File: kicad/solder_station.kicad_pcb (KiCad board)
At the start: 2 copper layers, 63.8 x 64 mm, 43 parts, among them IC1 ATMEGA328-P, P1 CONN_01X05, P2 CONN_01X02, P3 Standby, P4 UART, Q1 2N7000, Q2 IRF4905, U1 LM2596_module, U2 AD8551, U3 EC11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

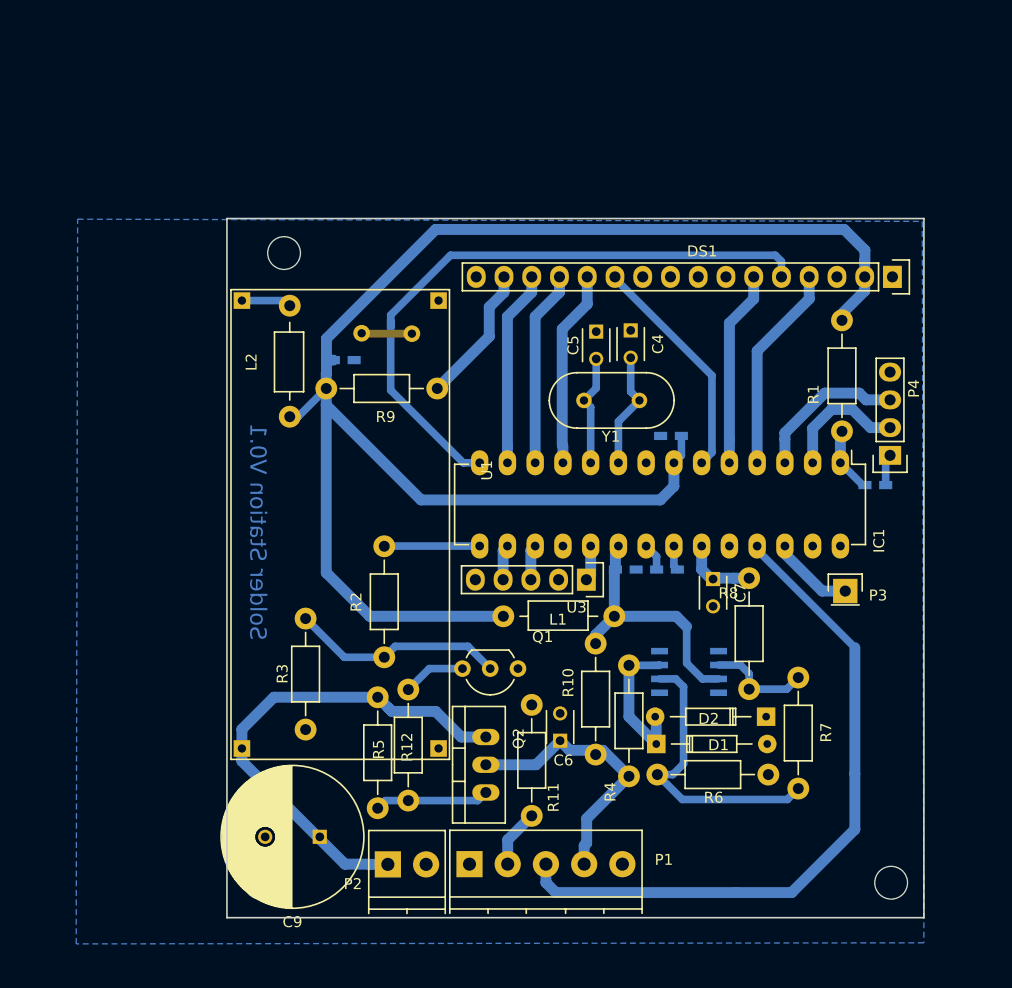
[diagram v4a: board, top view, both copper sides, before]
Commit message: [Kicad] Use more capacitors and smd parts
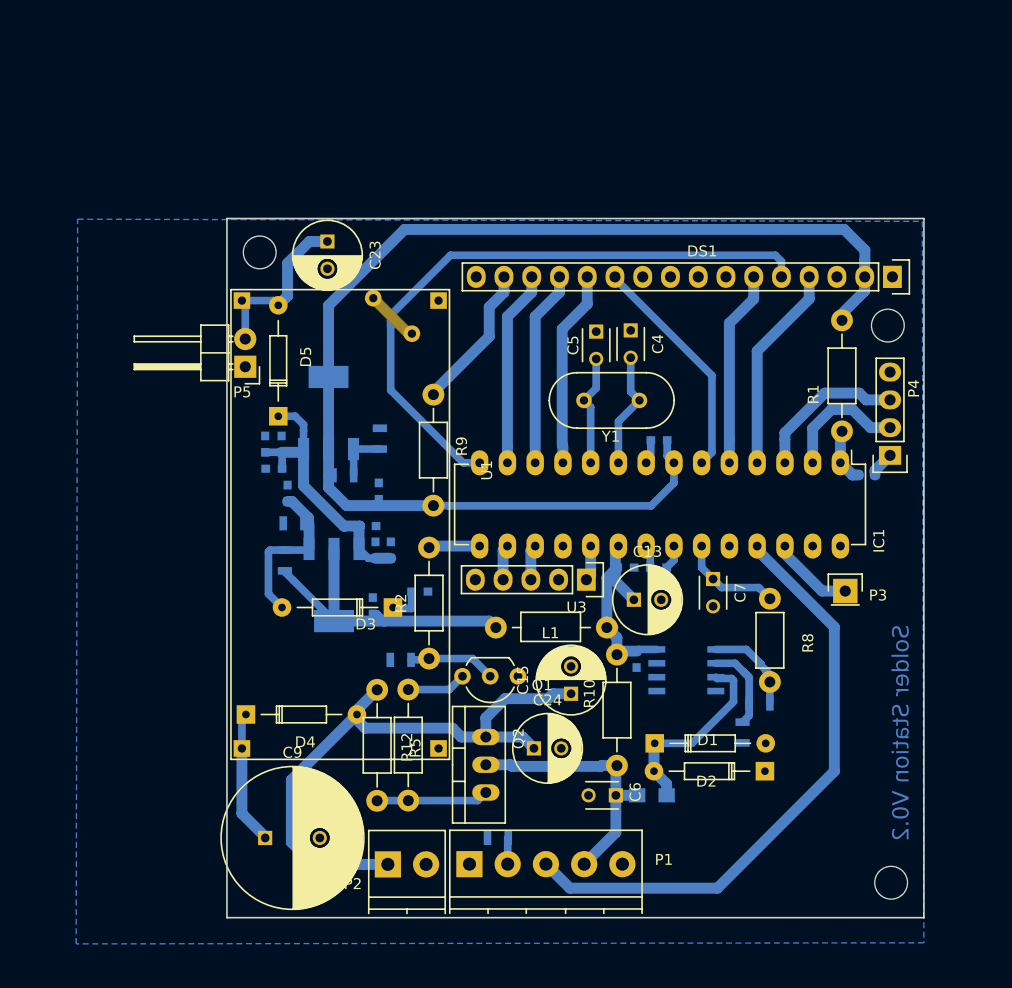
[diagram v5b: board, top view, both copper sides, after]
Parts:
- removed Hole2: MountingHole_3mm, Mounting_Holes:MountingHole_3mm
- removed L2: 10µH, Choke_Axial_ThroughHole:Choke_Horizontal_RM10mm
- added C11: 100nF, Capacitors_SMD:C_0603, B.Cu at (109.5, 84.7)
- added C12: 10µF, Capacitors_SMD:C_0603, B.Cu at (110.0, 89.2)
- added C13: CP, Capacitors_ThroughHole:C_Radial_D6.3_L11.2_P2.5, F.Cu at (141.8, 98.9)
- added C14: 100nF, Capacitors_SMD:C_0603, B.Cu at (142.0, 104.3)
- added C15: 1mF, Capacitors_ThroughHole:C_Radial_D6.3_L11.2_P2.5, F.Cu at (136.0, 107.5)
- added C16: 100nF, Capacitors_SMD:C_0603, B.Cu at (117.8, 99.5)
- added C17: 10µF, Capacitors_SMD:C_0603, B.Cu at (122.2, 98.2)
- added C18: 100nF, Capacitors_SMD:C_0603, B.Cu at (118.4, 89.0)
- added C19: 10µF, Capacitors_SMD:C_0603, B.Cu at (108.0, 84.7)
- added C20: 10µF, Capacitors_SMD:C_0603, B.Cu at (118.1, 94.3)
- added C21: 10µF, Capacitors_SMD:C_0603, B.Cu at (119.5, 94.3)
- added C22: 10µF, Capacitors_SMD:C_0603, B.Cu at (108.8, 86.9)
- added C23: 220µF, Capacitors_ThroughHole:C_Radial_D6.3_L11.2_P2.5, F.Cu at (113.7, 66.1)
- added C24: 1mF, Capacitors_ThroughHole:C_Radial_D6.3_L11.2_P2.5, F.Cu at (132.6, 112.5)
- added D3: D, Diodes_ThroughHole:Diode_DO-35_SOD27_Horizontal_RM10, F.Cu at (119.7, 99.6)
- added D4: D, Diodes_ThroughHole:Diode_DO-35_SOD27_Horizontal_RM10, F.Cu at (106.2, 109.4)
- added D5: D, Diodes_ThroughHole:Diode_DO-35_SOD27_Horizontal_RM10, F.Cu at (109.2, 82.1)
- added Hole1: MountingHole_3mm, Mounting_Holes:MountingHole_3mm, F.Cu at (165.0, 73.8)
- added P5: 12V_Out, Pin_Headers:Pin_Header_Angled_1x02, F.Cu at (106.2, 77.6)
- added R13: R, Resistors_SMD:R_0805, B.Cu at (118.5, 84.2)
- added R14: 240Ω, Resistors_SMD:R_0805, B.Cu at (115.2, 87.5)
- added R15: R, Resistors_SMD:R_0805, B.Cu at (110.6, 91.9)
- added R16: 240Ω, Resistors_SMD:R_0805, B.Cu at (109.8, 95.3)
- added U4: AMS1117, TO_SOT_Packages_SMD:SOT-223, B.Cu at (113.8, 81.8)
- added U5: AMS1117, TO_SOT_Packages_SMD:SOT-223, B.Cu at (114.3, 97.5)
- C1, C10, C2, C3, C8: footprint Capacitors_SMD:C_0603_HandSoldering -> Capacitors_SMD:C_0603
- C9: value CP -> 1mF
- R11, R3, R6, R7: footprint Resistors_ThroughHole:Resistor_Horizontal_RM10mm -> Resistors_SMD:R_0805; moved to B.Cu
- R4: footprint Resistors_ThroughHole:Resistor_Horizontal_RM10mm -> Resistors_SMD:R_0805_HandSoldering; moved to B.Cu
- R8: footprint Resistors_ThroughHole:Resistor_Horizontal_RM10mm -> Resistors_ThroughHole:Resistor_Horizontal_RM7mm
- U2: value AD8551 -> AD8572
- moved C10 15.3 mm to (117.4, 92.2), turned to 0 degrees
- moved R3 8.80 mm to (120.4, 104.4), turned to 180 degrees
- moved R11 7.75 mm to (129.3, 120.7), turned to 0 degrees
- moved R9 7.36 mm to (123.4, 85.2), turned to 270 degrees
- moved C6 7.14 mm to (140.1, 116.8), turned to 180 degrees
- moved R4 7.14 mm to (143.4, 116.8), turned to 180 degrees
- moved R5 5.76 mm to (118.2, 107.1)
- moved C9 5.00 mm to (108.0, 120.7), turned to 0 degrees
- moved D2 4.99 mm to (153.8, 114.6)
- moved R6 4.71 mm to (151.7, 111.0), turned to 270 degrees
- moved R7 4.46 mm to (153.2, 108.4), turned to 180 degrees
- moved R2 4.10 mm to (123.0, 99.2)
- moved R8 3.72 mm to (154.2, 98.8)
- moved REF**1 3.38 mm to (117.9, 71.3)
- moved Hole3 2.23 mm to (107.5, 67.1)
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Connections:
- C10 pad 1: GND -> +12VA
- C10 pad 2: +5V -> GND
- C9 pad 1: +24V -> Net-(C9-Pad1)
- L1 pad 1: +5V -> +5VA
- U1 pad 1: +24V -> Net-(C9-Pad1)
- U1 pad 3: Net-(L2-Pad2) -> +12V
- U2 pad 1: (no net) -> Net-(R7-Pad1)
- U2 pad 6: Net-(R7-Pad1) -> (no net)
- U2 pad 7: AVcc -> (no net)
- U2 pad 8: (no net) -> AVcc
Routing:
- net +5VA: track 0.00 -> 34.8 mm
- net +5V: track 146.4 -> 114.9 mm
- net +12VA: track 0.00 -> 25.4 mm
- net Net-(R6-Pad1): track 26.6 -> 8.32 mm
- net +12V: track 0.00 -> 15.8 mm
- net Net-(C12-Pad1): track 0.00 -> 15.2 mm
- net Net-(Q1-Pad2): track 19.9 -> 7.97 mm
- net Net-(C9-Pad1): track 0.00 -> 11.8 mm
- net +24V: track 45.5 -> 55.5 mm
- net /Button_connected: track 62.4 -> 55.6 mm
- net AVcc: track 23.7 -> 18.8 mm
- net Net-(R13-Pad1): track 0.00 -> 4.82 mm
- net Net-(L2-Pad2): track 4.57 -> 0.00 mm
- net Net-(D1-Pad1): track 13.6 -> 18.1 mm
- net /Heater_PWM: track 8.72 -> 4.69 mm
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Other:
- board text added: "Solder Station V0.2"
- board text removed: "Solder Station V0.1"

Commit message: [Kicad] Update (forgot to save).
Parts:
- moved C16 4.91 mm to (114.3, 102.9), turned to 0 degrees
- moved C24 1.92 mm to (134.3, 113.4)
- moved C6 1.24 mm to (139.8, 118.0)
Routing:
- net +5VA: track 34.8 -> 37.2 mm
- net /Heater+: track 24.3 -> 26.4 mm
- net +24V: track 55.5 -> 57.5 mm
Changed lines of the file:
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@@
     (thickness 1.6)
     (drawings 7)
-    (tracks 264)
+    (tracks 267)
     (zones 0)
     (modules 66)
@@
   )
   (setup
-    (last_trace_width 1)
+    (last_trace_width 0.7)
     (user_trace_width 0.7)
     (user_trace_width 1)
@@
   )
   (module Capacitors_ThroughHole:C_Disc_D3_P2.5 placed (layer F.Cu)
-    (at 140.1 116.8 180)
+    (at 139.8 118 180)
     (descr "Capacitor 3mm Disc, Pitch 2.5mm")
     (tags Capacitor)
@@
   )
   (module Capacitors_SMD:C_0603 (layer B.Cu)
-    (at 117.85 99.45 90)
+    (at 114.35 102.9)
     (descr "Capacitor SMD 0603, reflow soldering, AVX (see smccp.pdf)")
     (tags "capacitor 0603")
     (attr smd)
-    (fp_text reference C16 (at 0 1.9 90) (layer B.SilkS)
-      (effects (font (size 1 1) (thickness 0.15)) (justify mirror))
-    )
-    (fp_text value 100nF (at 0 -1.9 90) (layer B.Fab)
+    (fp_text reference C16 (at 0 1.9) (layer B.SilkS)
+      (effects (font (size 1 1) (thickness 0.15)) (justify mirror))
+    )
+    (fp_text value 100nF (at 0 -1.9) (layer B.Fab)
       (effects (font (size 1 1) (thickness 0.15)) (justify mirror))
     )
@@
     (fp_line (start -0.35 0.6) (end 0.35 0.6) (layer B.SilkS) (width 0.15))
     (fp_line (start 0.35 -0.6) (end -0.35 -0.6) (layer B.SilkS) (width 0.15))
-    (pad 1 smd rect (at -0.75 0 90) (size 0.8 0.75) (layers B.Cu B.Paste B.Mask)
+    (pad 1 smd rect (at -0.75 0) (size 0.8 0.75) (layers B.Cu B.Paste B.Mask)
       (net 36 +5VA))
-    (pad 2 smd rect (at 0.75 0 90) (size 0.8 0.75) (layers B.Cu B.Paste B.Mask)
+    (pad 2 smd rect (at 0.75 0) (size 0.8 0.75) (layers B.Cu B.Paste B.Mask)
       (net 14 GND))
     (model Capacitors_SMD.3dshapes/C_0603.wrl
@@
   )
   (module Capacitors_ThroughHole:C_Radial_D6.3_L11.2_P2.5 (layer F.Cu)
-    (at 132.6 112.5)
+    (at 134.3 113.4)
     (descr "Radial Electrolytic Capacitor, Diameter 6.3mm x Length 11.2mm, Pitch 2.5mm")
     (tags "Electrolytic Capacitor")
@@
   (segment (start 140.06 96.13) (end 140.06 94.255) (width 1) (layer B.Cu) (net 7))
   (segment (start 140.06 94.255) (end 140.335 93.98) (width 1) (layer B.Cu) (net 7))
-  (segment (start 132.6 112.5) (end 131.56 111.46) (width 1) (layer B.Cu) (net 8))
-  (segment (start 131.56 111.46) (end 128.2 111.46) (width 1) (layer B.Cu) (net 8))
+  (segment (start 134.3 113.4) (end 132.36 111.46) (width 1) (layer B.Cu) (net 8))
+  (segment (start 132.36 111.46) (end 128.2 111.46) (width 1) (layer B.Cu) (net 8))
   (segment (start 136 107.5) (end 134.35 107.5) (width 1) (layer B.Cu) (net 8))
   (segment (start 134.35 107.5) (end 133.9 107.95) (width 1) (layer B.Cu) (net 8))
@@
   (segment (start 155.575 84.21) (end 155.575 86.36) (width 1) (layer B.Cu) (net 25))
   (segment (start 155.575 83.624417) (end 155.575 84.21) (width 1) (layer B.Cu) (net 25))
-  (segment (start 140.2 114.08) (end 138.786508 114.08) (width 1) (layer B.Cu) (net 26))
-  (segment (start 138.786508 114.08) (end 138.716507 114.150001) (width 1) (layer B.Cu) (net 26))
-  (segment (start 138.716507 114.150001) (end 130.599681 114.150001) (width 1) (layer B.Cu) (net 26))
-  (segment (start 130.599681 114.150001) (end 130.44968 114) (width 1) (layer B.Cu) (net 26))
-  (segment (start 130.44968 114) (end 128.2 114) (width 1) (layer B.Cu) (net 26))
+  (segment (start 128.2 114) (end 130.44968 114) (width 1) (layer B.Cu) (net 26))
+  (segment (start 130.44968 114) (end 131.529169 115.079489) (width 1) (layer B.Cu) (net 26))
+  (segment (start 131.529169 115.079489) (end 139.200511 115.079489) (width 1) (layer B.Cu) (net 26))
+  (segment (start 139.200511 115.079489) (end 140.2 114.08) (width 1) (layer B.Cu) (net 26))
+  (segment (start 139.8 118) (end 139.8 117.1) (width 1) (layer B.Cu) (net 26))
+  (segment (start 139.8 117.1) (end 140.1 116.8) (width 1) (layer B.Cu) (net 26))
   (segment (start 140.1 116.8) (end 140.1 120.2) (width 1) (layer B.Cu) (net 26))
   (segment (start 140.1 120.2) (end 137.2 123.1) (width 1) (layer B.Cu) (net 26))
@@
   (segment (start 106.178 75.028) (end 106.178 71.818) (width 0.7) (layer B.Cu) (net 35))
   (segment (start 106.178 71.818) (end 105.87 71.51) (width 0.7) (layer B.Cu) (net 35))
+  (segment (start 113.6 102.9) (end 113.6 101.55) (width 0.7) (layer B.Cu) (net 36))
+  (segment (start 113.6 101.55) (end 114.3 100.85) (width 0.7) (layer B.Cu) (net 36))
   (segment (start 109.8 96.25) (end 109.8 96.35) (width 0.7) (layer B.Cu) (net 36))
   (segment (start 109.8 96.35) (end 110.6 97.15) (width 0.7) (layer B.Cu) (net 36))

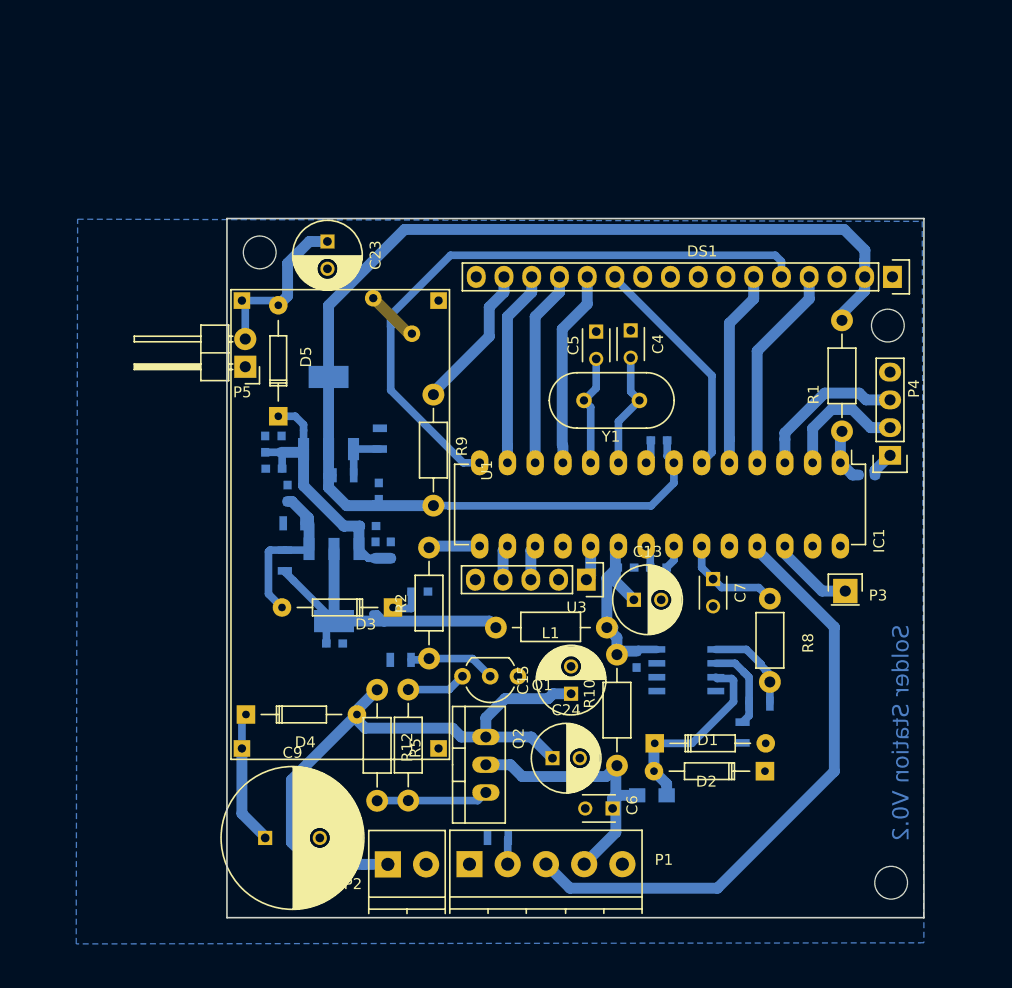
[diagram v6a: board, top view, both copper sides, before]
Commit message: [Kicad] Add a few more capacitors.
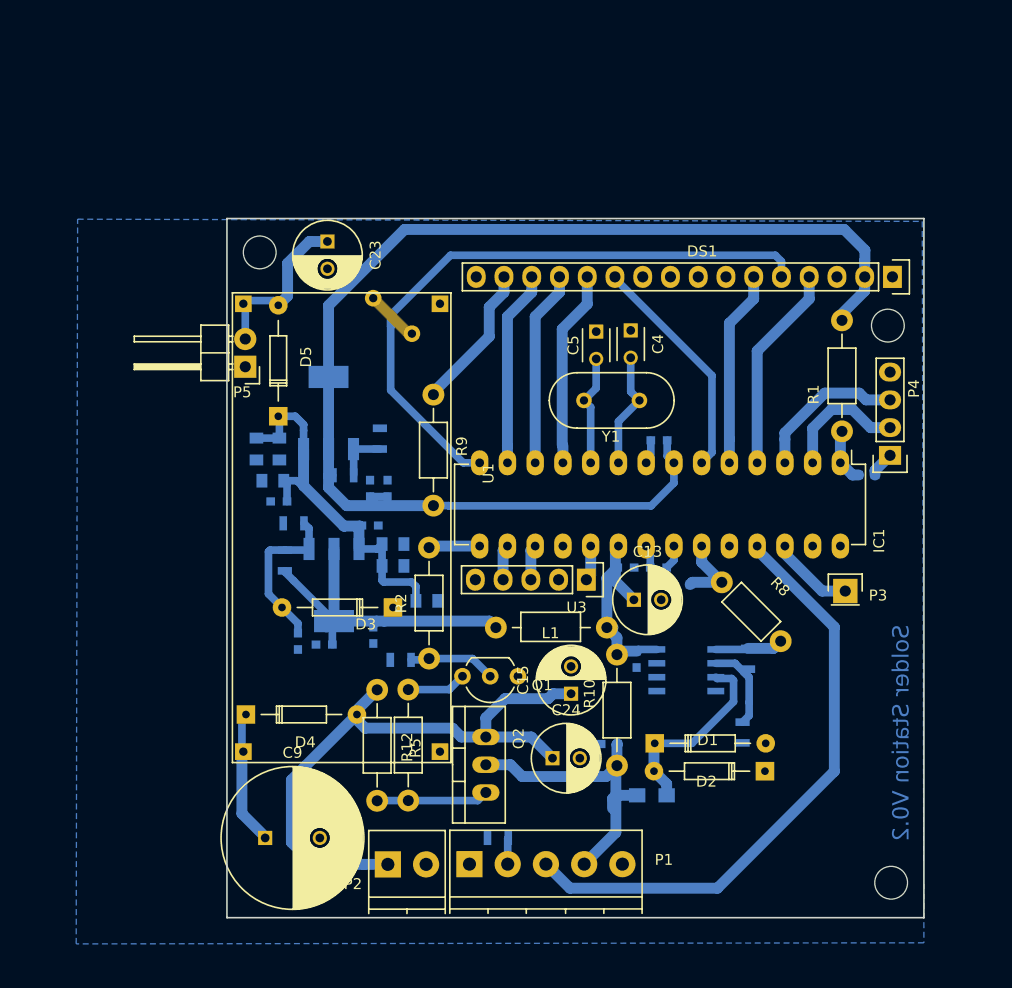
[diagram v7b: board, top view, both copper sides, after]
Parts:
- added C25: 10µF 16V, Capacitors_SMD:C_0805, B.Cu at (122.8, 99.0)
- added C26: 10µF 16V, Capacitors_SMD:C_0805, B.Cu at (109.3, 85.1)
- added C27: 10µF, Capacitors_SMD:C_0603, B.Cu at (119.2, 88.7)
- C19, C20, C21, C22: value 10µF -> 10µF 16V; footprint Capacitors_SMD:C_0603 -> Capacitors_SMD:C_0805
- C6, C7: footprint Capacitors_ThroughHole:C_Disc_D3_P2.5 -> Capacitors_SMD:C_0603; moved to B.Cu
- R13, R15: value R -> 300Ω
- R14: value 240Ω -> 100Ω
- moved C12 13.6 mm to (111.0, 102.7), turned to 270 degrees
- moved C22 12.9 mm to (119.7, 93.8), turned to 0 degrees
- moved C21 12.5 mm to (108.7, 88.0), turned to 180 degrees
- moved C11 11.0 mm to (117.6, 92.1), turned to 0 degrees
- moved C10 8.45 mm to (109.2, 89.9), turned to 180 degrees
- moved C6 5.91 mm to (139.5, 112.1)
- moved C17 5.84 mm to (117.9, 102.2), turned to 270 degrees
- moved R8 4.65 mm to (149.8, 97.3), turned to 315 degrees
- moved R7 4.23 mm to (152.2, 104.3), turned to 270 degrees
- moved C7 2.89 mm to (146.2, 97.5), turned to 180 degrees
- moved C20 2.16 mm to (119.7, 95.8), turned to 0 degrees
- moved C16 0.96 mm to (113.4, 103.0), turned to 180 degrees
- moved C19 0.92 mm to (107.2, 85.1), turned to 270 degrees
- moved C18 0.84 mm to (117.6, 88.7)
- moved U1 0.32 mm to (106.0, 112.8)
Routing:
- net +12VA: track 25.4 -> 36.3 mm
- net Net-(R7-Pad1): track 9.31 -> 6.25 mm
- net +5VA: track 37.2 -> 34.2 mm
- net /Temp_sense: track 9.85 -> 7.07 mm
- net +5V: track 114.9 -> 117.2 mm
- net /Heater+: track 26.4 -> 28.4 mm
